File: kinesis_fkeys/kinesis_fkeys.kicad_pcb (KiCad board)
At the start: 2 copper layers, 125.6 x 61 mm, 38 parts, among them J1 RIGHT_13_TOP, J3 LEFT_13_TOP

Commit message: finished second version of the layout
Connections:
- J1 pad 10: /right_fkeys/COL_5 -> /right_fkeys/COL_5_
- J1 pad 11: /right_fkeys/COL_5_ -> /right_fkeys/COL_5
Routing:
- removed copper zone on F.Cu, net /left_fkeys/ROW_F2
- removed copper zone on F.Cu, net /right_fkeys/ROW_ESC
- removed copper zone on B.Cu, net /right_fkeys/ROW_F2

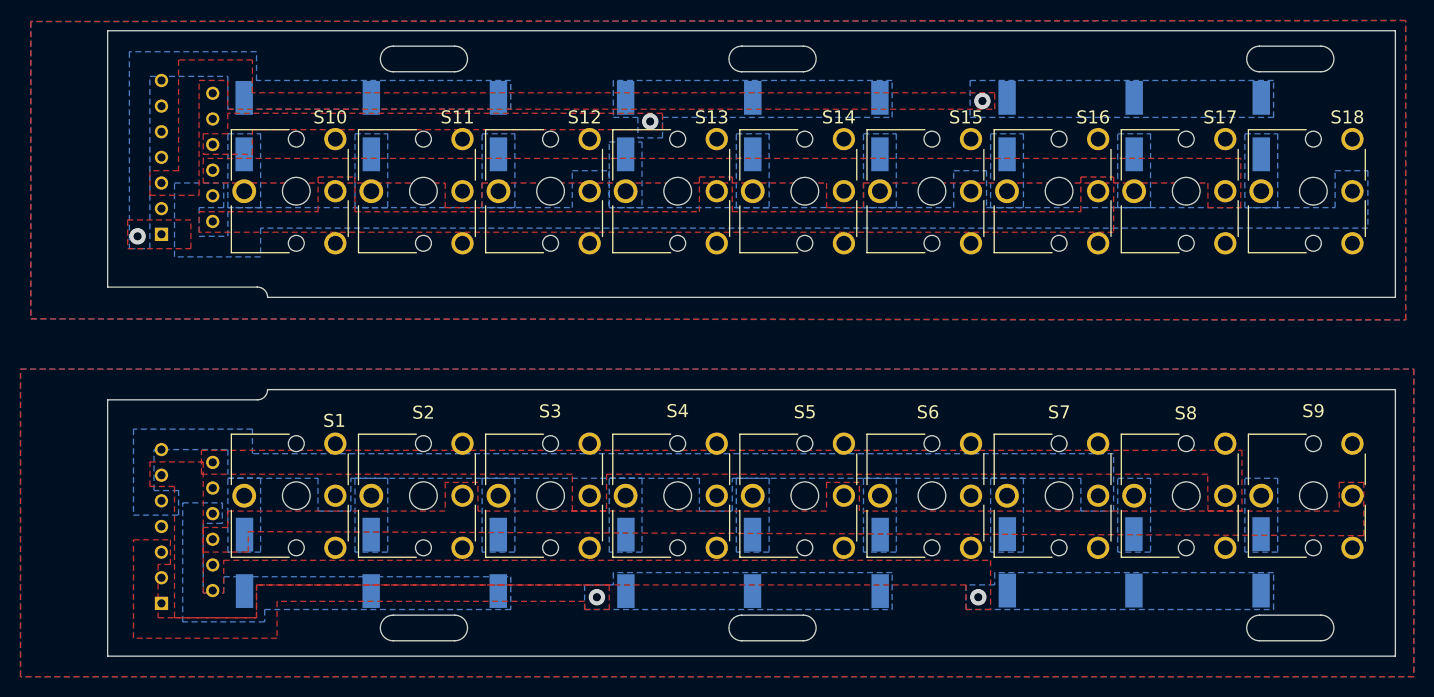
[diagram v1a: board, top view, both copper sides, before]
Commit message: finished layout with successful drc
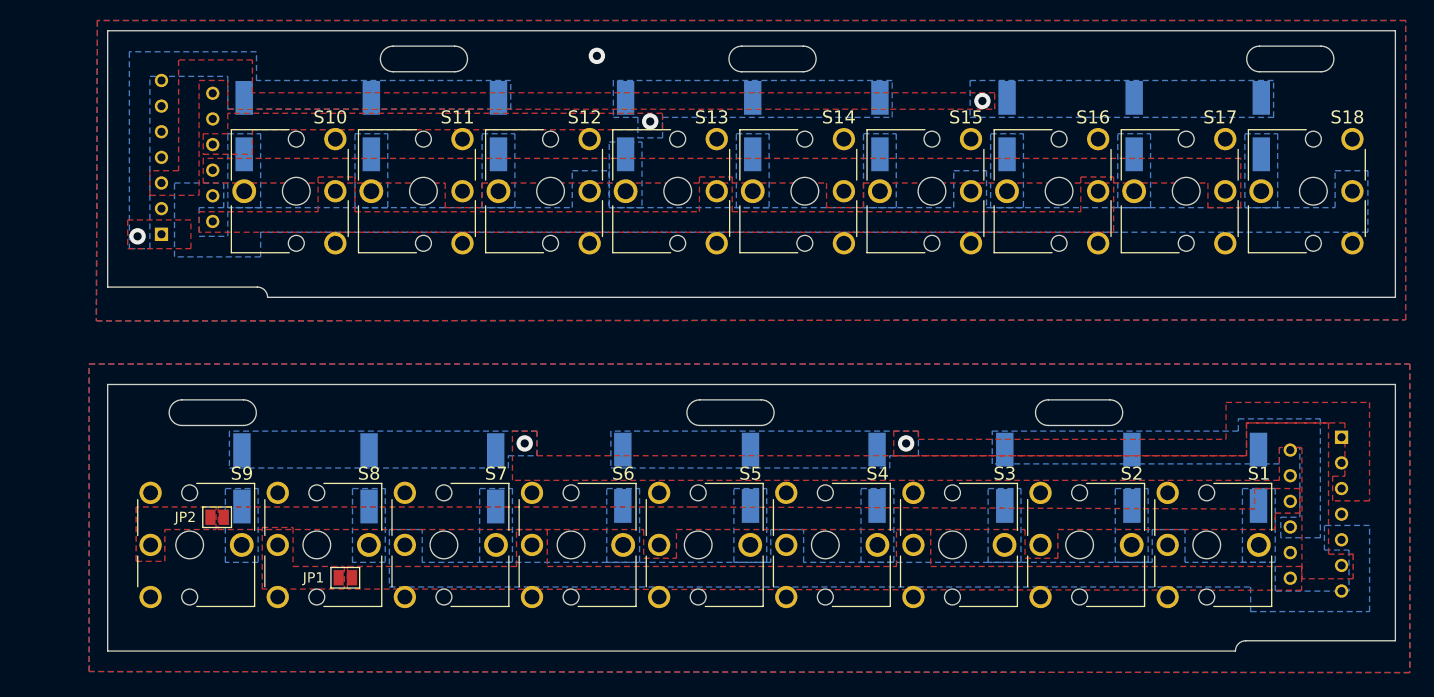
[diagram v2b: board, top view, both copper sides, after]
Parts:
- added JP1: SolderJumper_2_Open, Jumper:SolderJumper-2_P1.3mm_Open_Pad1.0x1.5mm, F.Cu at (117.4, 116.7)
- added JP2: SolderJumper_2_Open, Jumper:SolderJumper-2_P1.3mm_Open_Pad1.0x1.5mm, F.Cu at (104.9, 110.8)
- moved S9 118.2 mm to (98.4, 118.6), turned to 90 degrees
- moved J1 113.6 mm to (213.8, 110.3), turned to -90 degrees
- moved D9 99.7 mm to (107.3, 107.0), turned to -90 degrees
- moved D4 99.2 mm to (206.4, 106.9), turned to -90 degrees
- moved S8 93.6 mm to (110.8, 118.6), turned to 90 degrees
- moved S1 82.5 mm to (197.6, 118.6), turned to 90 degrees
- moved D8 75.0 mm to (119.7, 107.0), turned to -90 degrees
- moved D5 74.7 mm to (194.1, 106.9), turned to -90 degrees
- moved S7 69.3 mm to (123.2, 118.6), turned to 90 degrees
- moved S2 58.3 mm to (185.2, 118.6), turned to 90 degrees
- moved D7 50.6 mm to (132.0, 107.0), turned to -90 degrees
- moved D1 50.1 mm to (181.7, 106.9), turned to -90 degrees
- moved S6 45.4 mm to (135.6, 118.6), turned to 90 degrees
- moved S3 34.9 mm to (172.8, 118.6), turned to 90 degrees
- moved D6 26.4 mm to (144.4, 106.9), turned to -90 degrees
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- renumbered J3 to J2
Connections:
- S8 pad 2: /right_fkeys/ROW_F2 -> Net-(JP1-A)
- S9 pad 2: /right_fkeys/ROW_F1 -> Net-(JP2-A)
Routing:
- net GND_L: vias 0 -> 1
- added copper zone on F.Cu, net Net-(JP1-A)
- added copper zone on F.Cu, net Net-(JP2-A)
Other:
- board size 125.6 x 61 mm -> 125.6 x 60.5 mm
